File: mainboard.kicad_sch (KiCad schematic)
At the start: 86 parts, among them J1 Conn 02x05 1.27mm, J10 Conn -Z 02x05 2.00 mm, J11 Conn +X 02x05 2.00 mm, J12 Conn -X 02x05 2.00 mm, J2 USB_C_Receptacle_USB2.0, J3 Conn 02x10 1.27mm, J4 Conn +Z 02x05 2.00 mm, J5 Conn -Z 02x05 2.00 mm, J6 Conn +X 02x05 2.00 mm, J7 Conn -X 02x05 2.00 mm, J8 U.FL-R-SMT-1, J9 Conn +Z 02x05 2.00 mm, Q1 DMG2301L, SW1 KMR231NG, U1 ATSAMD51J20A-M, U10 USBLC6-2SC6, U2 MAX706RESA+, U3 AP2112K-3.3, U4 MR25H40, U5 BMX160, U6 RFM98PW, U7 DRV8830DRC, U8 DRV8830DRC, U9 DRV8830DRC, Y1 32.768kHz

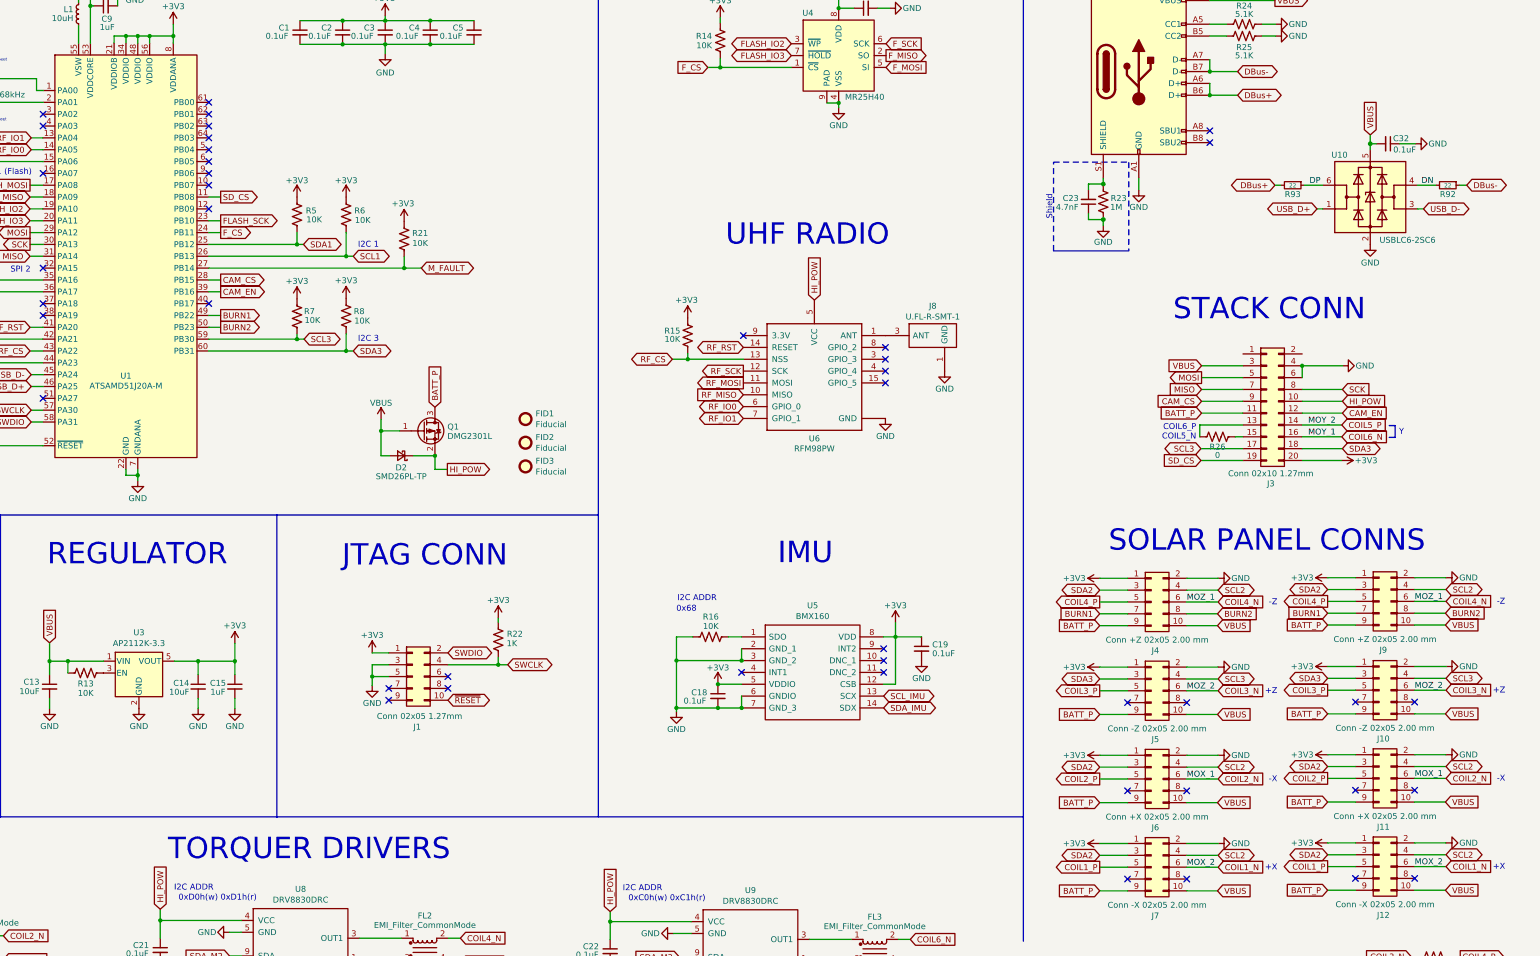
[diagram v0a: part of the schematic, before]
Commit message: Grounded Mounting Holes
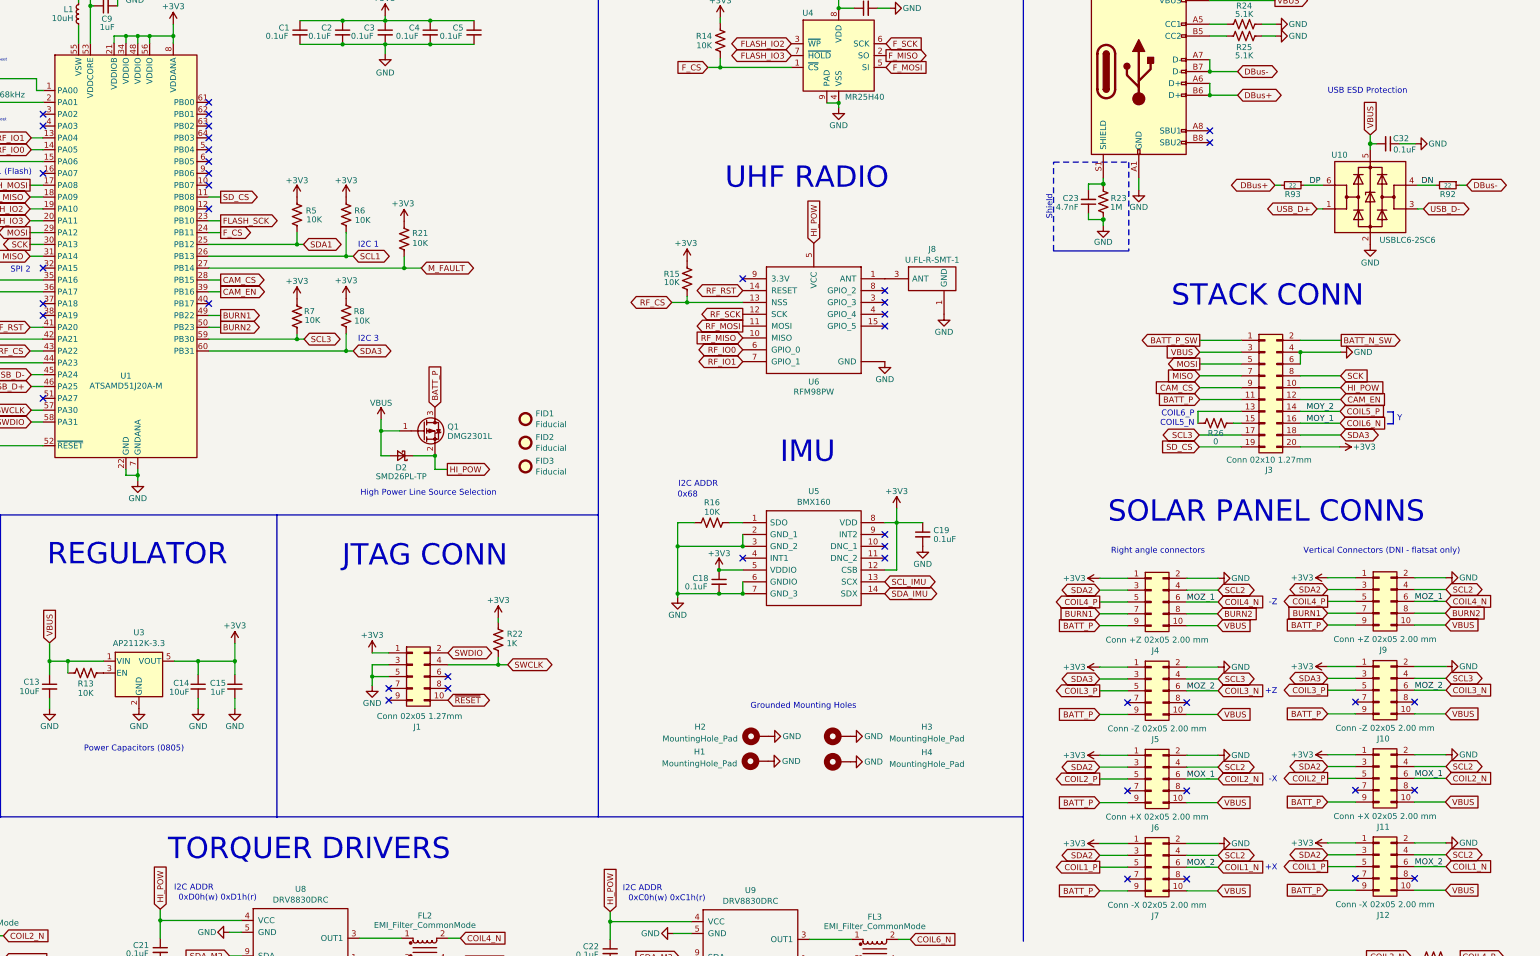
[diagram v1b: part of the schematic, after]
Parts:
- added H1, H2, H3, H4: MountingHole_Pad, MountingHole:MountingHole_2.2mm_M2_Pad, symbol Mechanical:MountingHole_Pad
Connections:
- net GND: now also H1.1, H2.1, H3.1, H4.1
- net BATT_P_SW: now reaches J3.1 (Pin_1)
- net BATT_N_SW: now reaches J3.2 (Pin_2)
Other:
- note added: "Grounded Mounting Holes"
- note added: "High Power Line Source Selection"
- note added: "Power Capacitors (0805)"
- note added: "Right angle connectors"
- note added: "USB ESD Protection"
- note added: "Vertical Connectors (DNI - flatsat only)"
- moved on the sheet: C18, C19, J3, J8, R15, R16, R26, U5, U6

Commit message: Suggested changes
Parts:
- H1, H2, H3, H4: footprint MountingHole:MountingHole_2.2mm_M2_Pad -> mainboard:MountingHole
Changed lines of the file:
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@@
     (property "Reference" "H4" (id 0) (at 291.211 194.945 90))
     (property "Value" "MountingHole_Pad" (id 1) (at 291.211 197.4819 90))
-    (property "Footprint" "MountingHole:MountingHole_2.2mm_M2_Pad" (id 2) (at 272.288 196.977 0)
+    (property "Footprint" "mainboard:MountingHole" (id 2) (at 272.288 196.977 0)
       (effects (font (size 1.27 1.27)) hide)
     )
@@
     (property "Reference" "H2" (id 0) (at 242.57 189.4871 90))
     (property "Value" "MountingHole_Pad" (id 1) (at 242.57 192.024 90))
-    (property "Footprint" "MountingHole:MountingHole_2.2mm_M2_Pad" (id 2) (at 254.762 191.516 0)
+    (property "Footprint" "mainboard:MountingHole" (id 2) (at 254.762 191.516 0)
       (effects (font (size 1.27 1.27)) hide)
     )
@@
     (property "Reference" "H3" (id 0) (at 291.211 189.484 90))
     (property "Value" "MountingHole_Pad" (id 1) (at 291.211 192.0209 90))
-    (property "Footprint" "MountingHole:MountingHole_2.2mm_M2_Pad" (id 2) (at 272.288 191.516 0)
+    (property "Footprint" "mainboard:MountingHole" (id 2) (at 272.288 191.516 0)
       (effects (font (size 1.27 1.27)) hide)
     )
@@
     (property "Reference" "H1" (id 0) (at 242.443 194.818 90))
     (property "Value" "MountingHole_Pad" (id 1) (at 242.443 197.3549 90))
-    (property "Footprint" "MountingHole:MountingHole_2.2mm_M2_Pad" (id 2) (at 254.635 196.85 0)
+    (property "Footprint" "mainboard:MountingHole" (id 2) (at 254.635 196.85 0)
       (effects (font (size 1.27 1.27)) hide)
     )
@@
     )
     (path "/be70f136-d7a1-4a45-a623-206a0192b120"
-      (reference "H1") (unit 1) (value "MountingHole_Pad") (footprint "MountingHole:MountingHole_2.2mm_M2_Pad")
+      (reference "H1") (unit 1) (value "MountingHole_Pad") (footprint "mainboard:MountingHole")
     )
     (path "/2ae7110c-dd57-44eb-8578-38ecb356be67"
-      (reference "H2") (unit 1) (value "MountingHole_Pad") (footprint "MountingHole:MountingHole_2.2mm_M2_Pad")
+      (reference "H2") (unit 1) (value "MountingHole_Pad") (footprint "mainboard:MountingHole")
     )
     (path "/7043636c-fc7a-4113-a97b-b2f47f3dd9ea"
-      (reference "H3") (unit 1) (value "MountingHole_Pad") (footprint "MountingHole:MountingHole_2.2mm_M2_Pad")
+      (reference "H3") (unit 1) (value "MountingHole_Pad") (footprint "mainboard:MountingHole")
     )
     (path "/0b4843f9-5d68-4dcb-8869-ee4088e9fddf"
-      (reference "H4") (unit 1) (value "MountingHole_Pad") (footprint "MountingHole:MountingHole_2.2mm_M2_Pad")
+      (reference "H4") (unit 1) (value "MountingHole_Pad") (footprint "mainboard:MountingHole")
     )
     (path "/d317bf52-6f3f-41bf-8364-424160d9ec15"

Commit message: Some changes plus new step file
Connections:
- net BATT_P: now also Q1.2 (S); no longer Q1.3 (D)
- net HI_POW: now also Q1.3 (D); no longer Q1.2 (S)
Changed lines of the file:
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@@
     (pin "1")
   )
-  (symbol (lib_id "Transistor_FET:DMG2301L") (at 183.134 125.984 0) (unit 1)
+  (symbol (lib_id "Transistor_FET:DMG2301L") (at 183.134 125.984 0) (mirror x) (unit 1)
     (in_bom yes) (on_board yes)
-    (property "Reference" "Q1" (id 0) (at 188.341 125.095 0)
+    (property "Reference" "Q1" (id 0) (at 188.341 126.873 0)
       (effects (font (size 1.27 1.27)) (justify left))
     )
-    (property "Value" "DMG2301L" (id 1) (at 188.341 127.127 0)
+    (property "Value" "DMG2301L" (id 1) (at 188.341 124.841 0)
       (effects (font (size 1.27 1.27)) (justify left))
     )
-    (property "Footprint" "Package_TO_SOT_SMD:SOT-23" (id 2) (at 188.214 127.889 0)
+    (property "Footprint" "Package_TO_SOT_SMD:SOT-23" (id 2) (at 188.214 124.079 0)
       (effects (font (size 1.27 1.27) italic) (justify left) hide)
     )

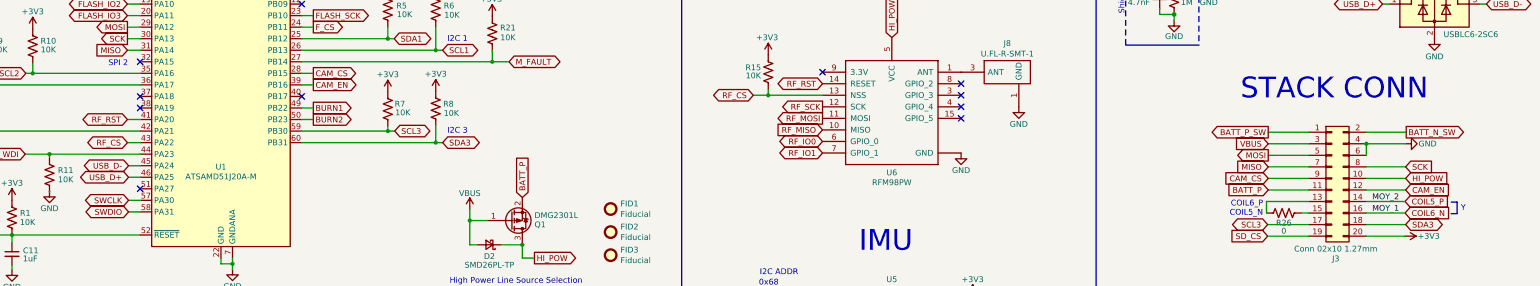
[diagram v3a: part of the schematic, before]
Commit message: Firmware updates for ATSAMD51J19A
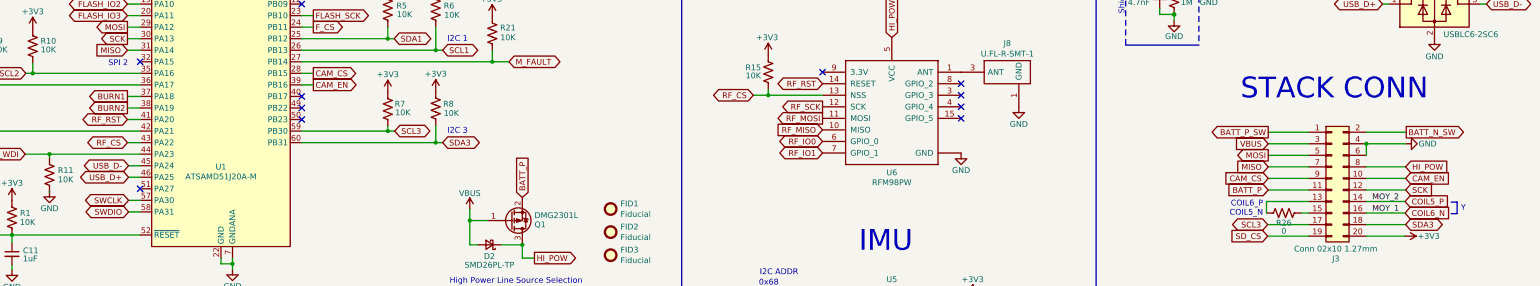
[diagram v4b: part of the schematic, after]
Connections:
- net BURN1: now also U1.37 (PA18); no longer U1.49 (PB22)
- net BURN2: now also U1.38 (PA19); no longer U1.50 (PB23)
- net CAM_EN: now also J3.10 (Pin_10); no longer J3.12 (Pin_12)
- net HI_POW: now also J3.8 (Pin_8); no longer J3.10 (Pin_10)
- net SCK: now also J3.12 (Pin_12); no longer J3.8 (Pin_8)
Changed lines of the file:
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@@
   (no_connect (at 351.917 64.135))
   (no_connect (at 188.468 178.689))
-  (no_connect (at 101.6 101.219))
-  (no_connect (at 101.6 98.679))
   (no_connect (at 101.6 91.059))
   (no_connect (at 40.513 106.299))
   (no_connect (at 346.964 203.2))
   (no_connect (at 395.859 184.15))
+  (no_connect (at 137.16 101.219))
+  (no_connect (at 137.16 103.759))
   (no_connect (at 137.16 78.359))
   (no_connect (at 101.6 118.999))
@@
     (stroke (width 0) (type default) (color 0 0 0 0))
   )
-  (wire (pts (xy 139.7 103.759) (xy 137.16 103.759))
+  (wire (pts (xy 98.806 101.219) (xy 101.6 101.219))
     (stroke (width 0) (type default) (color 0 0 0 0))
   )
@@
     (stroke (width 0) (type default) (color 0 0 0 0))
   )
-  (wire (pts (xy 139.7 101.219) (xy 137.16 101.219))
+  (wire (pts (xy 98.806 98.679) (xy 101.6 98.679))
     (stroke (width 0) (type default) (color 0 0 0 0))
   )
@@
     )
   )
-  (global_label "CAM_EN" (shape input) (at 379.984 119.253 0) (fields_autoplaced)
-    (effects (font (size 1.27 1.27)) (justify left))
-    (property "Intersheet References" "${INTERSHEET_REFS}" (id 0) (at 389.5653 119.1736 0)
-      (effects (font (size 1.27 1.27)) (justify left) hide)
-    )
-  )
-  (global_label "BURN1" (shape output) (at 139.7 101.219 0) (fields_autoplaced)
-    (effects (font (size 1.27 1.27)) (justify left))
-    (property "Intersheet References" "${INTERSHEET_REFS}" (id 0) (at 41.91 -122.301 0)
+  (global_label "CAM_EN" (shape input) (at 379.984 116.713 0) (fields_autoplaced)
+    (effects (font (size 1.27 1.27)) (justify left))
+    (property "Intersheet References" "${INTERSHEET_REFS}" (id 0) (at 389.5653 116.6336 0)
+      (effects (font (size 1.27 1.27)) (justify left) hide)
+    )
+  )
+  (global_label "BURN1" (shape output) (at 98.806 98.679 180) (fields_autoplaced)
+    (effects (font (size 1.27 1.27)) (justify right))
+    (property "Intersheet References" "${INTERSHEET_REFS}" (id 0) (at 196.596 322.199 0)
       (effects (font (size 1.27 1.27)) hide)
     )
@@
     )
   )
-  (global_label "BURN2" (shape output) (at 139.7 103.759 0) (fields_autoplaced)
-    (effects (font (size 1.27 1.27)) (justify left))
-    (property "Intersheet References" "${INTERSHEET_REFS}" (id 0) (at 41.91 -122.301 0)
+  (global_label "BURN2" (shape output) (at 98.806 101.219 180) (fields_autoplaced)
+    (effects (font (size 1.27 1.27)) (justify right))
+    (property "Intersheet References" "${INTERSHEET_REFS}" (id 0) (at 196.596 327.279 0)
       (effects (font (size 1.27 1.27)) hide)
     )
@@
     )
   )
-  (global_label "SCK" (shape input) (at 379.984 114.173 0) (fields_autoplaced)
-    (effects (font (size 1.27 1.27)) (justify left))
-    (property "Intersheet References" "${INTERSHEET_REFS}" (id 0) (at 104.394 -114.427 0)
+  (global_label "SCK" (shape input) (at 379.984 119.253 0) (fields_autoplaced)
+    (effects (font (size 1.27 1.27)) (justify left))
+    (property "Intersheet References" "${INTERSHEET_REFS}" (id 0) (at 104.394 -109.347 0)
       (effects (font (size 1.27 1.27)) hide)
     )
@@
     )
   )
-  (global_label "HI_POW" (shape input) (at 379.984 116.713 0) (fields_autoplaced)
-    (effects (font (size 1.27 1.27)) (justify left))
-    (property "Intersheet References" "${INTERSHEET_REFS}" (id 0) (at 389.263 116.6336 0)
-      (effects (font (size 1.27 1.27)) (justify left) hide)
-    )
+  (global_label "HI_POW" (shape input) (at 379.984 114.173 0) (fields_autoplaced)
+    (effects (font (size 1.27 1.27)) (justify left))
+    (property "Intersheet References" "${INTERSHEET_REFS}" (id 0) (at 389.263 114.0936 0)
+      (effects (font (size 1.27 1.27)) (justify left) hide)
+    )
